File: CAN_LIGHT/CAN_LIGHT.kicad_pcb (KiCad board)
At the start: 2 copper layers, 135.5 x 115.4 mm, 190 parts, among them J1 Conn_ARM_SWD_TagConnect_TC2030, J2 436500428, J3 430450428, J4 Conn_ARM_SWD_TagConnect_TC203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, U1 MSPM0C1103SDDFR, U5 XMSM0G3507SDGS28R

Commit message: Mionr routing
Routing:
- net +5V: track 776.6 -> 793.2 mm
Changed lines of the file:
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@@
   (segment (start 169.529436 47.894564) (end 171.45 49.276) (width 0.3048) (layer "F.Cu") (net 3))
   (segment (start 165.481 43.18) (end 167.135047 42.181258) (width 0.3048) (layer "F.Cu") (net 3))
+  (segment (start 88.204631 110.392095) (end 88.646 109.3724) (width 0.3048) (layer "F.Cu") (net 3))
   (segment (start 126.238 127.635) (end 134.366 130.175) (width 1.3208) (layer "F.Cu") (net 3))
   (segment (start 176.046493 52.729493) (end 175.949013 53.158987) (width 0.3048) (layer "F.Cu") (net 3))
@@
   (segment (start 118.813714 122.923473) (end 117.983 124.968) (width 1.3208) (layer "F.Cu") (net 3))
   (segment (start 69.696524 91.226265) (end 67.564 91.567) (width 1.3208) (layer "F.Cu") (net 3))
+  (segment (start 82.671917 107.856221) (end 82.9056 106.934) (width 0.25) (layer "B.Cu") (net 3))
+  (segment (start 95.668182 112.849683) (end 96.105408 111.955008) (width 0.25) (layer "B.Cu") (net 3))
+  (segment (start 90.7796 110.1852) (end 88.138 109.22) (width 0.25) (layer "B.Cu") (net 3))
+  (segment (start 99.0092 112.6236) (end 96.3676 111.8108) (width 0.25) (layer "B.Cu") (net 3))
+  (segment (start 87.898393 109.335993) (end 88.138 109.22) (width 0.25) (layer "B.Cu") (net 3))
+  (segment (start 87.495492 110.147919) (end 87.898393 109.335993) (width 0.25) (layer "B.Cu") (net 3))
+  (segment (start 96.3676 111.8108) (end 96.105408 111.955008) (width 0.25) (layer "B.Cu") (net 3))
+  (segment (start 90.568428 111.206016) (end 90.7796 110.1852) (width 0.25) (layer "B.Cu") (net 3))
+  (segment (start 79.701949 106.386606) (end 80.3656 105.5116) (width 0.25) (layer "B.Cu") (net 3))
+  (segment (start 98.759116 113.853988) (end 99.0092 112.6236) (width 0.25) (layer "B.Cu") (net 3))
+  (segment (start 82.9056 106.934) (end 81.28 106.0196) (width 0.25) (layer "B.Cu") (net 3))
+  (segment (start 82.516532 108.011606) (end 82.671917 107.856221) (width 0.25) (layer "B.Cu") (net 3))
+  (segment (start 80.3656 105.5116) (end 81.28 106.0196) (width 0.25) (layer "B.Cu") (net 3))
   (segment (start 90.297 112.8268) (end 89.685416 111.863584) (width 0.254) (layer "F.Cu") (net 8))
   (segment (start 90.297 112.8268) (end 92.329 113.538) (width 0.254) (layer "F.Cu") (net 8))

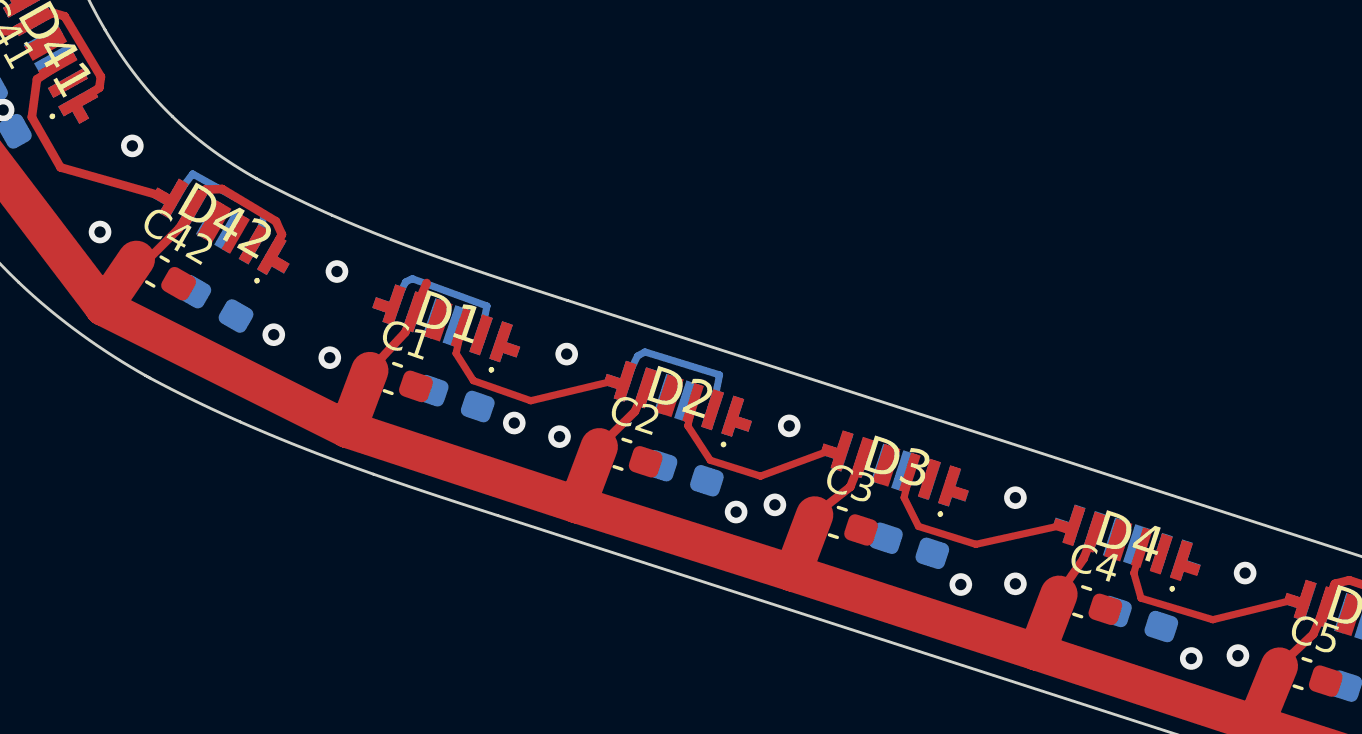
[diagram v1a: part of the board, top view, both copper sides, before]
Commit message: Route top level 5V
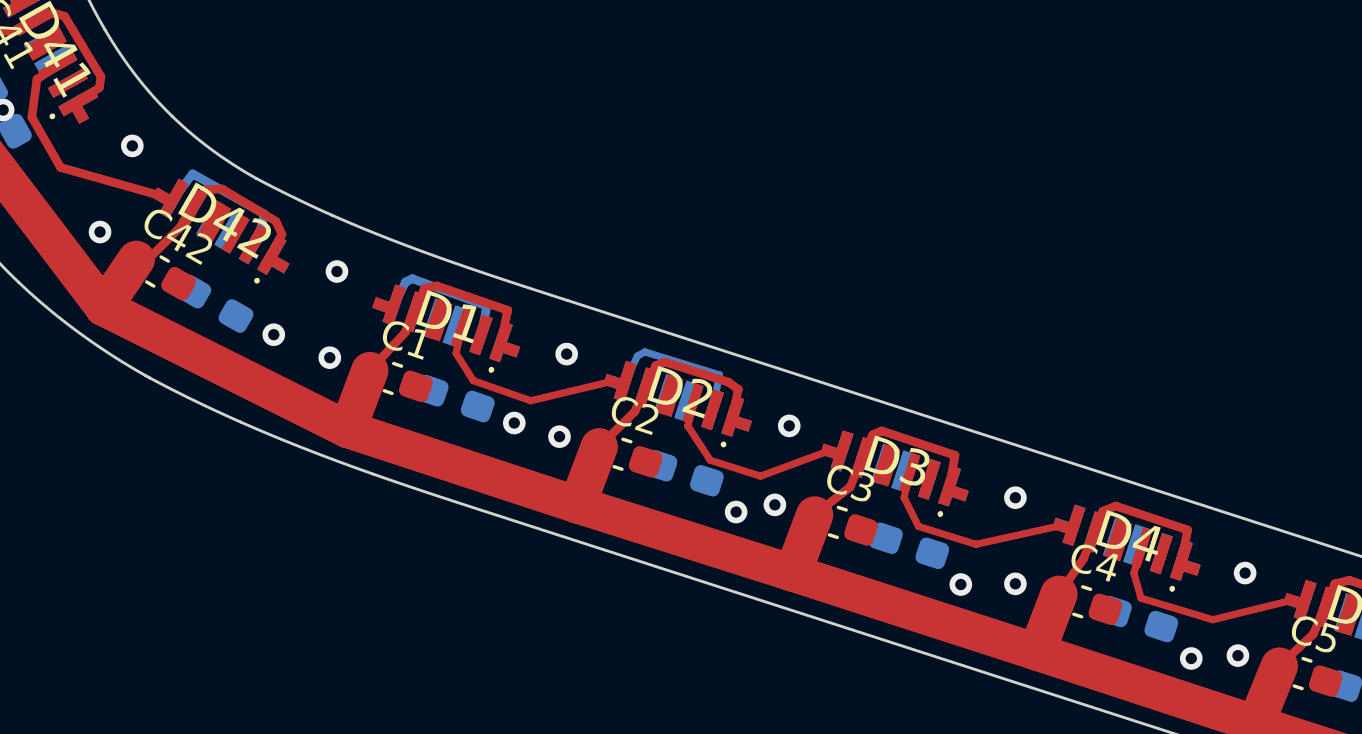
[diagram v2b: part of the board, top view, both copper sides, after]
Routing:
- net +5V: track 793.2 -> 812.4 mm

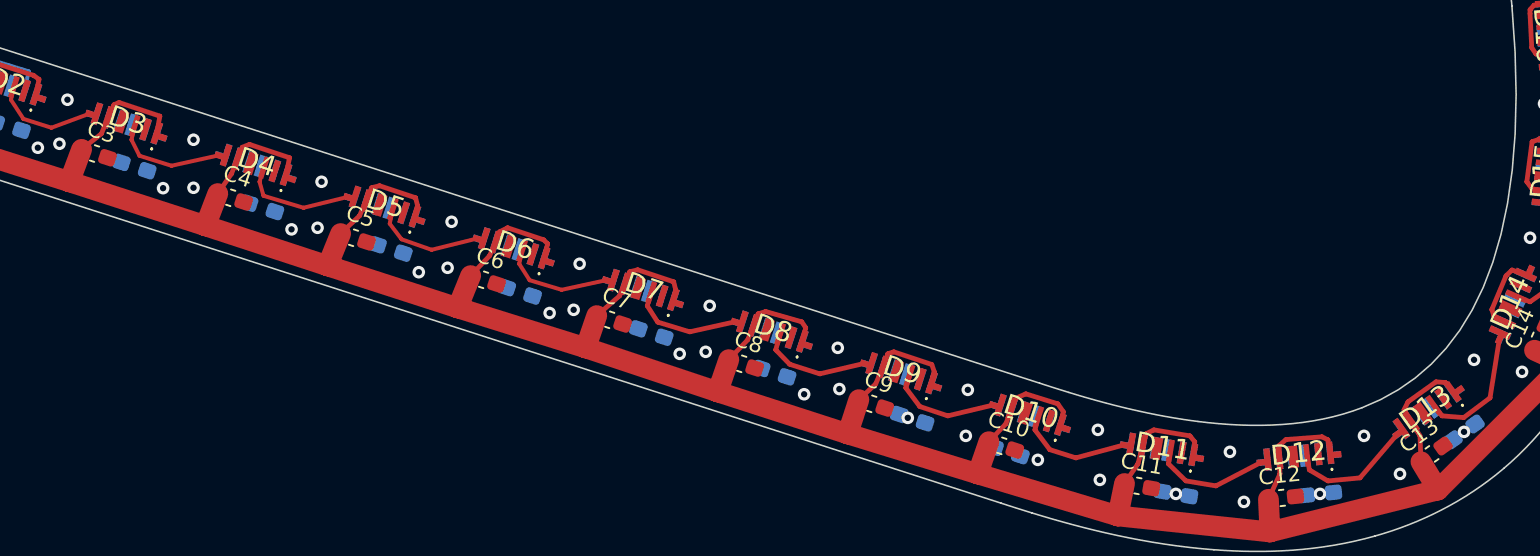
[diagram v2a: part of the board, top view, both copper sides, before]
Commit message: Route some of bottom level 5V
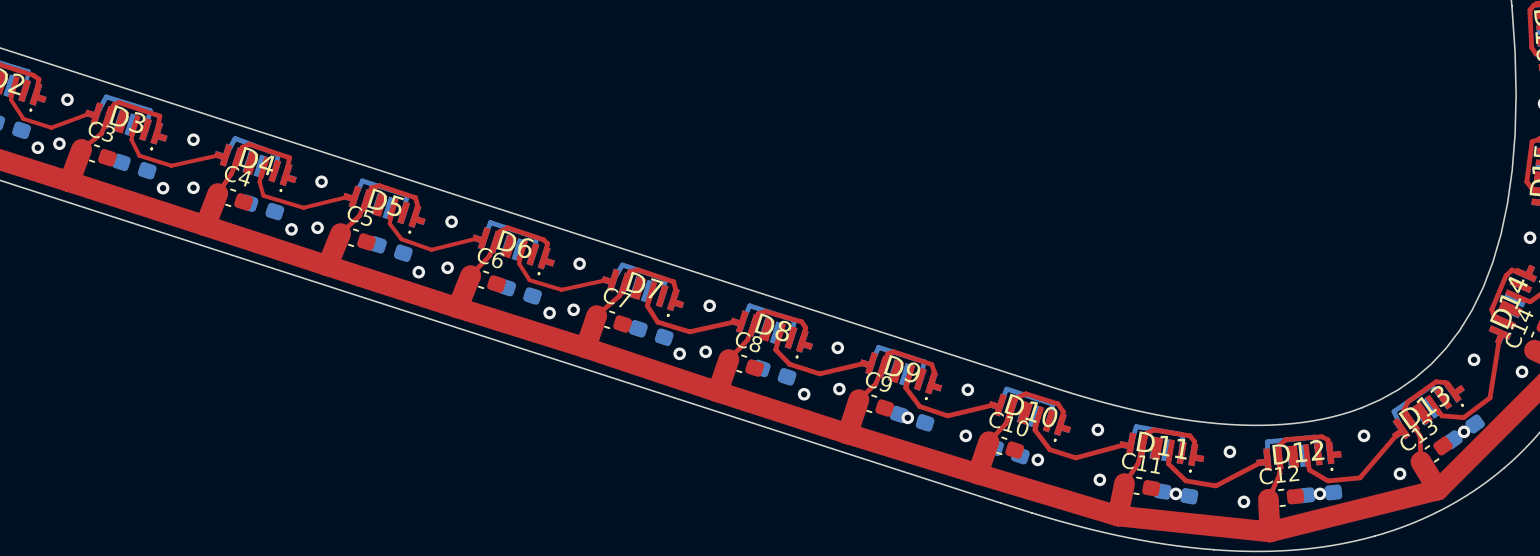
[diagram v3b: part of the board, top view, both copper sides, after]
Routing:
- net +5V: track 812.4 -> 870.1 mm
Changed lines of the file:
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@@
   (segment (start 118.813714 122.923473) (end 117.983 124.968) (width 1.3208) (layer "F.Cu") (net 3))
   (segment (start 69.696524 91.226265) (end 67.564 91.567) (width 1.3208) (layer "F.Cu") (net 3))
+  (segment (start 144.78 127.508) (end 144.314684 128.527978) (width 0.3048) (layer "B.Cu") (net 3))
+  (segment (start 139.446 125.8316) (end 136.7028 124.9172) (width 0.3048) (layer "B.Cu") (net 3))
+  (segment (start 120.1928 119.5832) (end 119.727484 120.603178) (width 0.3048) (layer "B.Cu") (net 3))
   (segment (start 82.671917 107.856221) (end 82.9056 106.934) (width 0.3048) (layer "B.Cu") (net 3))
+  (segment (start 185.674 134.2136) (end 186.14311 135.30923) (width 0.3048) (layer "B.Cu") (net 3))
+  (segment (start 188.0616 132.588) (end 185.674 134.2136) (width 0.3048) (layer "B.Cu") (net 3))
+  (segment (start 139.221316 126.884188) (end 139.446 125.8316) (width 0.3048) (layer "B.Cu") (net 3))
+  (segment (start 180.6448 135.8392) (end 177.6476 136.144) (width 0.3048) (layer "B.Cu") (net 3))
+  (segment (start 147.405618 129.532283) (end 147.6248 128.4224) (width 0.3048) (layer "B.Cu") (net 3))
   (segment (start 95.668182 112.849683) (end 96.105408 111.955008) (width 0.25) (layer "B.Cu") (net 3))
+  (segment (start 147.6248 128.4224) (end 144.78 127.508) (width 0.3048) (layer "B.Cu") (net 3))
+  (segment (start 114.8588 117.9068) (end 112.1156 116.8908) (width 0.3048) (layer "B.Cu") (net 3))
+  (segment (start 122.818418 121.607483) (end 123.0376 120.4976) (width 0.3048) (layer "B.Cu") (net 3))
+  (segment (start 155.609818 132.173883) (end 155.8544 131.064) (width 0.3048) (layer "B.Cu") (net 3))
+  (segment (start 128.3208 122.2248) (end 127.926182 123.238283) (width 0.3048) (layer "B.Cu") (net 3))
+  (segment (start 131.017116 124.242588) (end 131.2672 123.19) (width 0.3048) (layer "B.Cu") (net 3))
+  (segment (start 180.867458 136.923444) (end 180.6448 135.8392) (width 0.3048) (layer "B.Cu") (net 3))
+  (segment (start 172.18908 136.837422) (end 172.2628 135.6868) (width 0.3048) (layer "B.Cu") (net 3))
+  (segment (start 188.788985 133.421945) (end 188.0616 132.588) (width 0.3048) (layer "B.Cu") (net 3))
+  (segment (start 103.9368 114.2492) (end 103.344484 115.319978) (width 0.3048) (layer "B.Cu") (net 3))
+  (segment (start 163.788618 134.815483) (end 164.0332 133.7564) (width 0.3048) (layer "B.Cu") (net 3))
+  (segment (start 114.639618 118.940483) (end 114.8588 117.9068) (width 0.3048) (layer "B.Cu") (net 3))
   (segment (start 90.7796 110.1852) (end 88.138 109.22) (width 0.3048) (layer "B.Cu") (net 3))
   (segment (start 99.0092 112.6236) (end 96.3676 111.8108) (width 0.25) (layer "B.Cu") (net 3))
+  (segment (start 172.2628 135.6868) (end 169.3164 135.1788) (width 0.3048) (layer "B.Cu") (net 3))
+  (segment (start 136.7028 124.9172) (end 136.130382 125.879883) (width 0.3048) (layer "B.Cu") (net 3))
+  (segment (start 164.0332 133.7564) (end 161.0868 132.7912) (width 0.3048) (layer "B.Cu") (net 3))
   (segment (start 87.898393 109.335993) (end 88.138 109.22) (width 0.3048) (layer "B.Cu") (net 3))
+  (segment (start 161.0868 132.7912) (end 160.697684 133.811178) (width 0.3048) (layer "B.Cu") (net 3))
+  (segment (start 112.1156 116.8908) (end 111.548684 117.936178) (width 0.3048) (layer "B.Cu") (net 3))
   (segment (start 87.495492 110.147919) (end 87.898393 109.335993) (width 0.3048) (layer "B.Cu") (net 3))
+  (segment (start 152.9588 130.1496) (end 152.518884 131.169578) (width 0.3048) (layer "B.Cu") (net 3))
   (segment (start 96.3676 111.8108) (end 96.105408 111.955008) (width 0.25) (layer "B.Cu") (net 3))
+  (segment (start 123.0376 120.4976) (end 120.1928 119.5832) (width 0.3048) (layer "B.Cu") (net 3))
+  (segment (start 106.435418 116.324283) (end 106.7308 115.1128) (width 0.3048) (layer "B.Cu") (net 3))
+  (segment (start 131.2672 123.19) (end 128.3208 122.2248) (width 0.3048) (layer "B.Cu") (net 3))
+  (segment (start 106.7308 115.1128) (end 103.9368 114.2492) (width 0.3048) (layer "B.Cu") (net 3))
   (segment (start 90.568428 111.206016) (end 90.7796 110.1852) (width 0.3048) (layer "B.Cu") (net 3))
   (segment (start 79.701949 106.386606) (end 80.3656 105.5116) (width 0.3048) (layer "B.Cu") (net 3))
+  (segment (start 155.8544 131.064) (end 152.9588 130.1496) (width 0.3048) (layer "B.Cu") (net 3))
   (segment (start 98.759116 113.853988) (end 99.0092 112.6236) (width 0.25) (layer "B.Cu") (net 3))
   (segment (start 82.9056 106.934) (end 81.28 106.0196) (width 0.3048) (layer "B.Cu") (net 3))
   (segment (start 82.516532 108.011606) (end 82.671917 107.856221) (width 0.3048) (layer "B.Cu") (net 3))
   (segment (start 80.3656 105.5116) (end 81.28 106.0196) (width 0.3048) (layer "B.Cu") (net 3))
+  (segment (start 169.3164 135.1788) (end 168.988455 136.273065) (width 0.3048) (layer "B.Cu") (net 3))
+  (segment (start 177.6476 136.144) (end 177.635262 137.263161) (width 0.3048) (layer "B.Cu") (net 3))
   (segment (start 90.297 112.8268) (end 89.685416 111.863584) (width 0.254) (layer "F.Cu") (net 8))
   (segment (start 90.297 112.8268) (end 92.329 113.538) (width 0.254) (layer "F.Cu") (net 8))
